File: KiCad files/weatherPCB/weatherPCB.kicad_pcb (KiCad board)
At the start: 2 copper layers, 54.9 x 61.1 mm, 33 parts, among them J1 Expansion header, J3 USB_C_Receptacle_USB2.0_16P, SW1 RESET, SW2 BOOT, U1 OPT3001DNPR, U16 ESP32-S3-WROOM-1, U17 USBLC6-2SC6, U18 BME280, U19 LM1117DT-ADJ

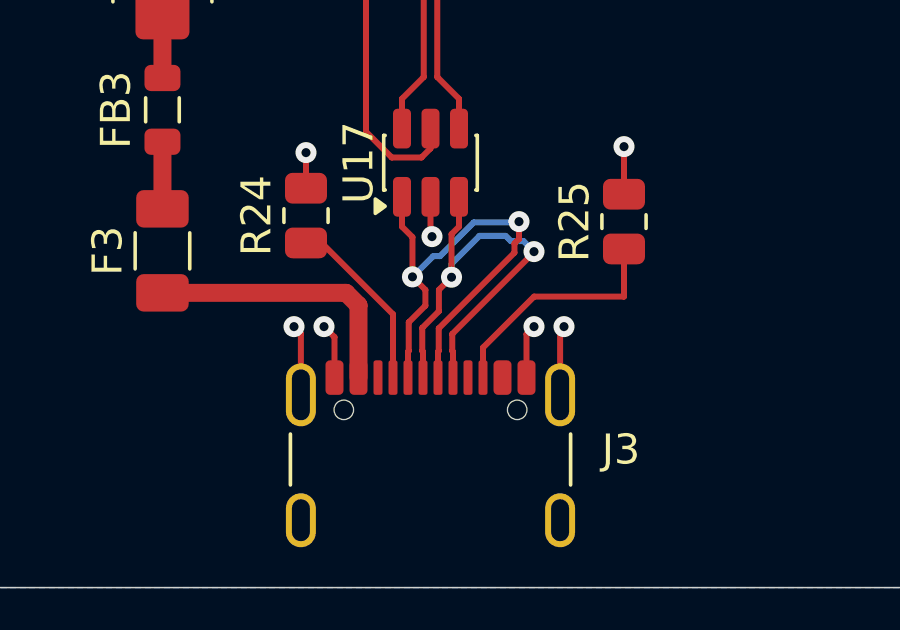
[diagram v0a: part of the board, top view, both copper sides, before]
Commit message: Improved usb routing on pcb
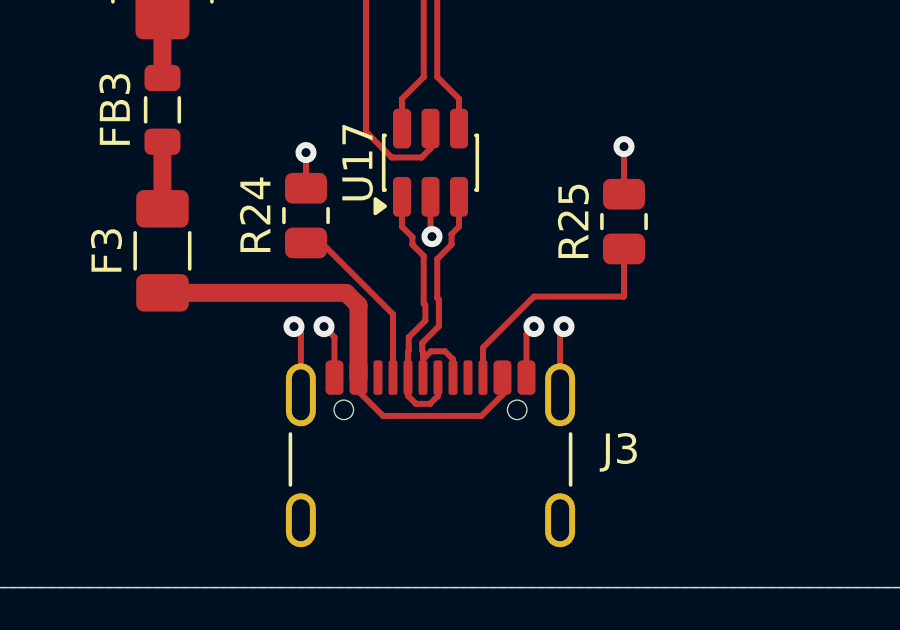
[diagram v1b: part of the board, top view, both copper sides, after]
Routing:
- net /D-: track 17.6 -> 9.39 mm, vias 2 -> 0
- net /D+: track 16.3 -> 9.53 mm, vias 2 -> 0
- net Net-(F3-Pad1): track 9.12 -> 15.6 mm

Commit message: replaced bme280 with bme680
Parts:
- removed U18: BME280, Package_LGA:Bosch_LGA-8_2.5x2.5mm_P0.65mm_ClockwisePinNumbering
- added U2: BME680, Package_LGA:Bosch_LGA-8_3x3mm_P0.8mm_ClockwisePinNumbering, F.Cu at (136.0, 114.0)
- turned C1 to 90 degrees
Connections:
- C1 pad 1: /EN -> GND
- C1 pad 2: GND -> /EN
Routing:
- net SCL: track 54.3 -> 60.0 mm
- net SDA: track 73.6 -> 78.9 mm
